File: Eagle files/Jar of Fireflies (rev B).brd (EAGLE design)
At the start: 81.3 x 81.3 mm, 18 parts, among them IC1 ATTINY85, J1 POWER_JACKPTH, J3 M02PTH, J4 M02PTH

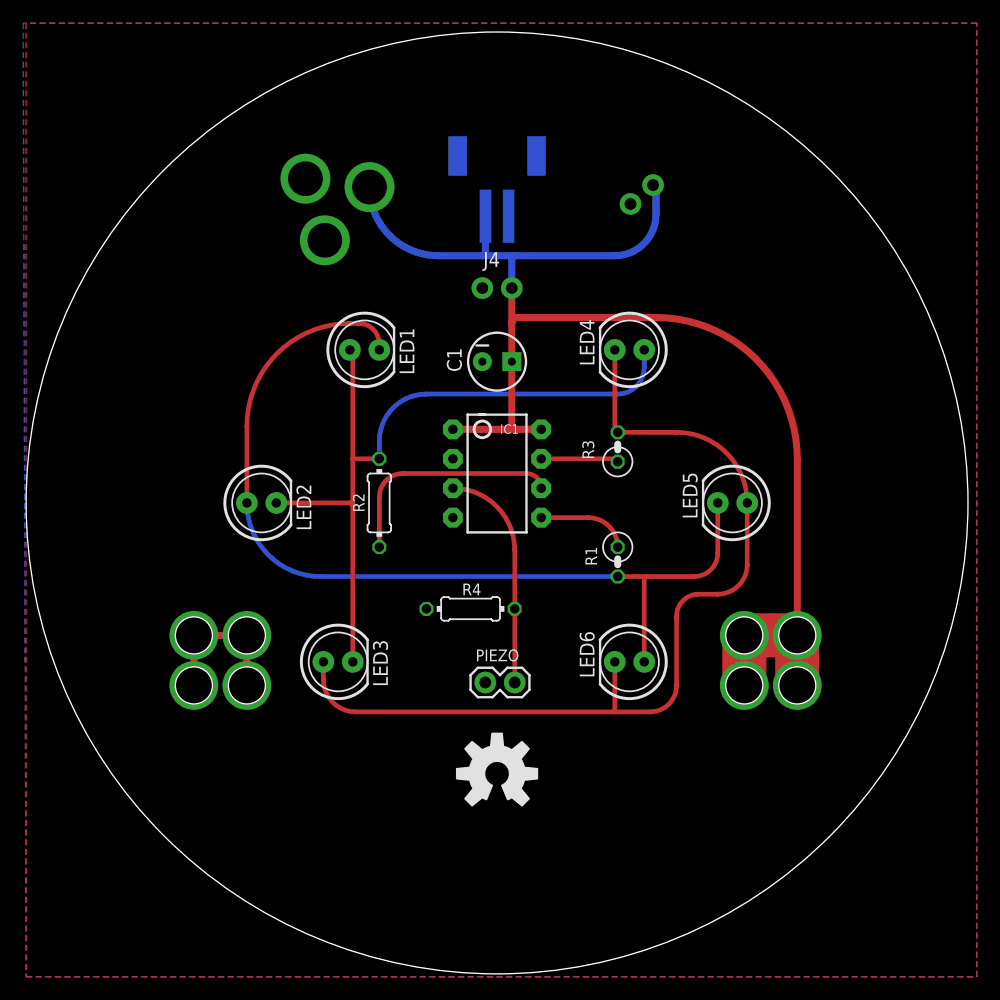
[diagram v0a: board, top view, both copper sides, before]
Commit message: Updated Eagle files
Better silkscreen, more power options.
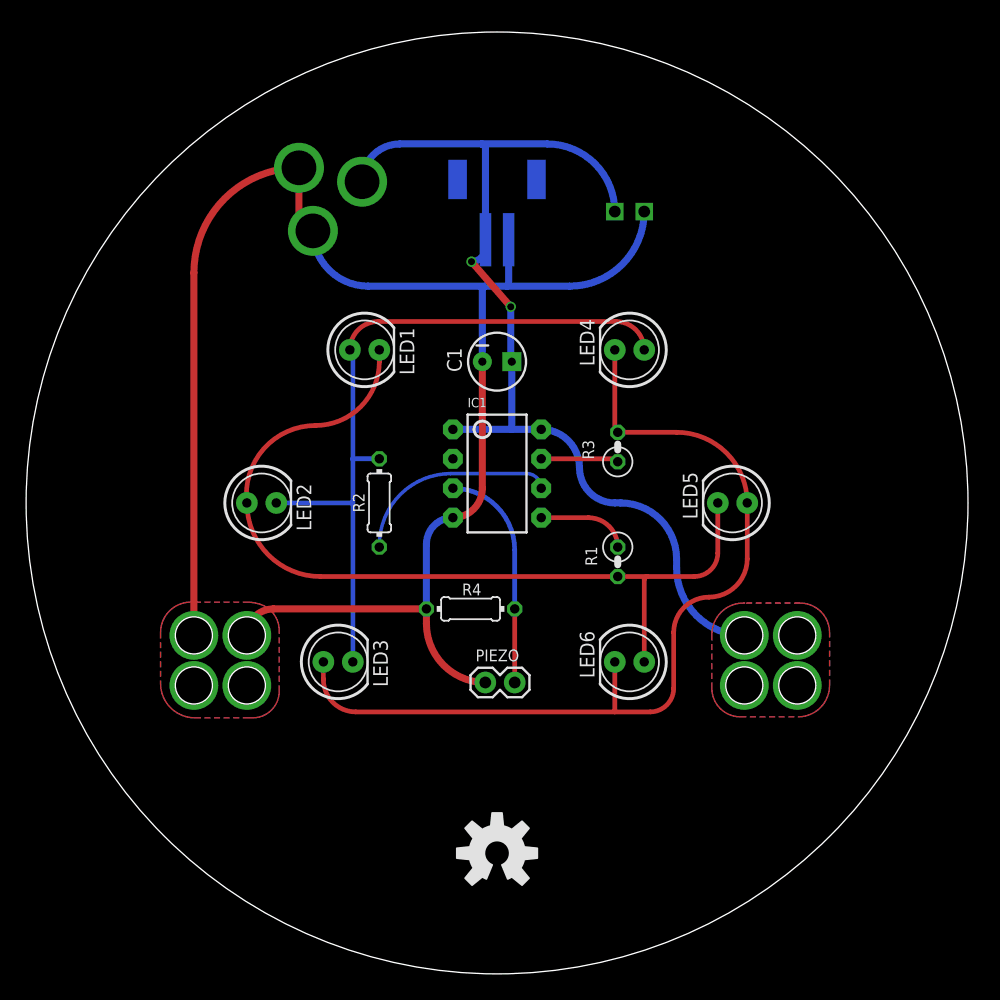
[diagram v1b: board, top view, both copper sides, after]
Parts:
- removed J4: M02PTH, SparkFun-Connectors:1X02
- J3: value M02PTH -> M022.54MM_SCREWTERM; device SparkFun-Connectors:1X02 -> SparkFun-Connectors:1X02_2.54_SCREWTERM
- R1, R2, R3: value 100 -> 150
- moved LOGO1 6.86 mm to (40.6, 10.4)
- moved J3 2.41 mm to (53.3, 65.8), turned to 0 degrees
- moved J2 2.03 mm to (40.6, 67.1)
- moved J1 1.98 mm to (19.3, 58.7), turned to 45 degrees
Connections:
- net GND: now also J3.P2; no longer J3.2, J4.2
- net VCC: now also J3.P1; no longer J3.1, J4.1
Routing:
- net GND: track 13.2 -> 142.2 mm
- net VCC: track 115.9 -> 85.6 mm, vias 4 -> 6
- net N$2: track 78.9 -> 73.6 mm
- net PORTB: track 19.7 -> 17.2 mm
- net N$1: track 64.6 -> 63.3 mm
- net N$3: track 78.6 -> 77.6 mm
- added copper zone on layer 1, net VCC
- added copper zone on layer 16, net VCC
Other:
- board text removed: "Designed by Jason Webb"
- board text removed: "FIREFLIES"
- board text removed: "JAR OF"
- board text removed: "http://jason-webb.info"
